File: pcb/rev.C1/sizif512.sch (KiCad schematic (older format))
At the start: 186 parts, among them J1 DS-210, J10 RCJ-014, J11 PinHeader, J12 PJ-313, J13 PinHeader, J14 PinHeader, J15 PJ-313, J16 MEM2055-00-190-01-A, J17 PinHeader, J2 Conn_02x28_Row_Letter_First, J3 PinHeader, J4 DS1020-08, J5 DS1020-05, J6 PinHeader, J7 DB9-M, J8 PinHeader, J9 Mini-DIN-9, Q1 BC547C, Q2 BC547C, Q3 BC547C, Q4 BC547C, SW1 Jumper, SW2 Button THT, SW3 Button THT, U1 LM2596T-ADJ, U10 SN74CB3T3245PW, U11 AD724, U12 AS6C4008-55PCN, U13 74HCT4053D, U14 AY-3-8910, U15 LM311N, U2 AMS1117-3.3, U3 SN74CB3T3245PW, U4 Z84C0010PEC, U5 SN74CB3T3245PW, U6 EPM1270T144, U7 SN74CB3T3245PW, U8 SST39SF040, U9 74HCU04, Y1 28 MHz, Y2 4.433 MHz

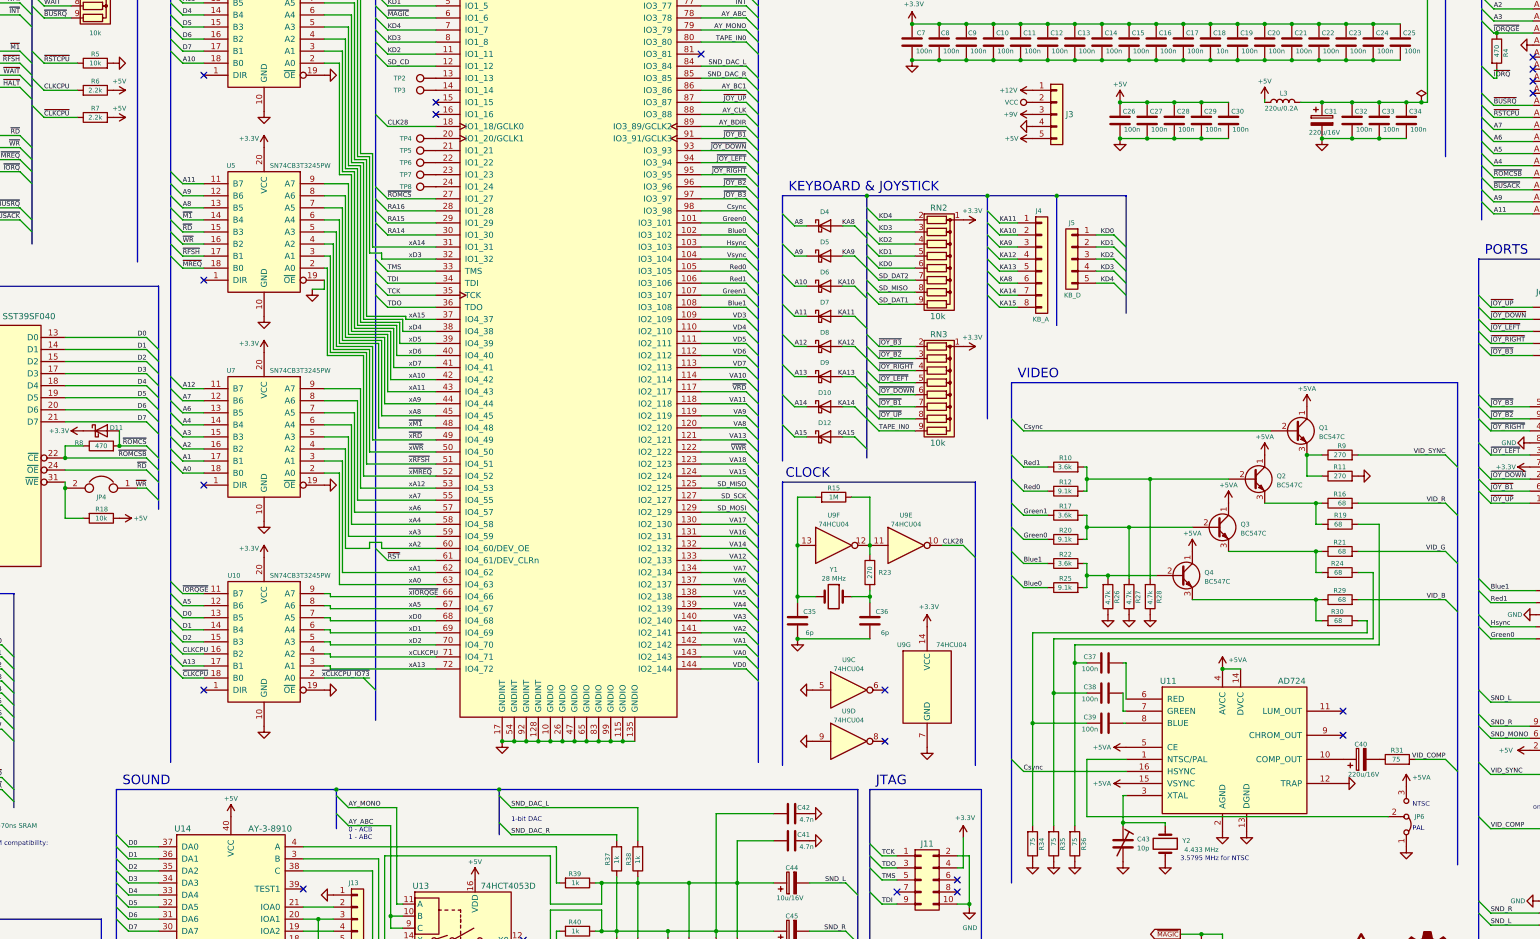
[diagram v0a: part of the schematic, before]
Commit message: pcb rev.C1: minor values change
Video circuit tuning:
R10, R17, R22, R26, R27, R27: 1.5k
R12, R20, R25: 3k
C43: 30p (wider range is better)
Q1, Q2, Q3, Q4: BC549B (low noise, less amplification)

Exclude 2.2k value from BOM:
R6, R7: 2k

Also add some assembly drawing.
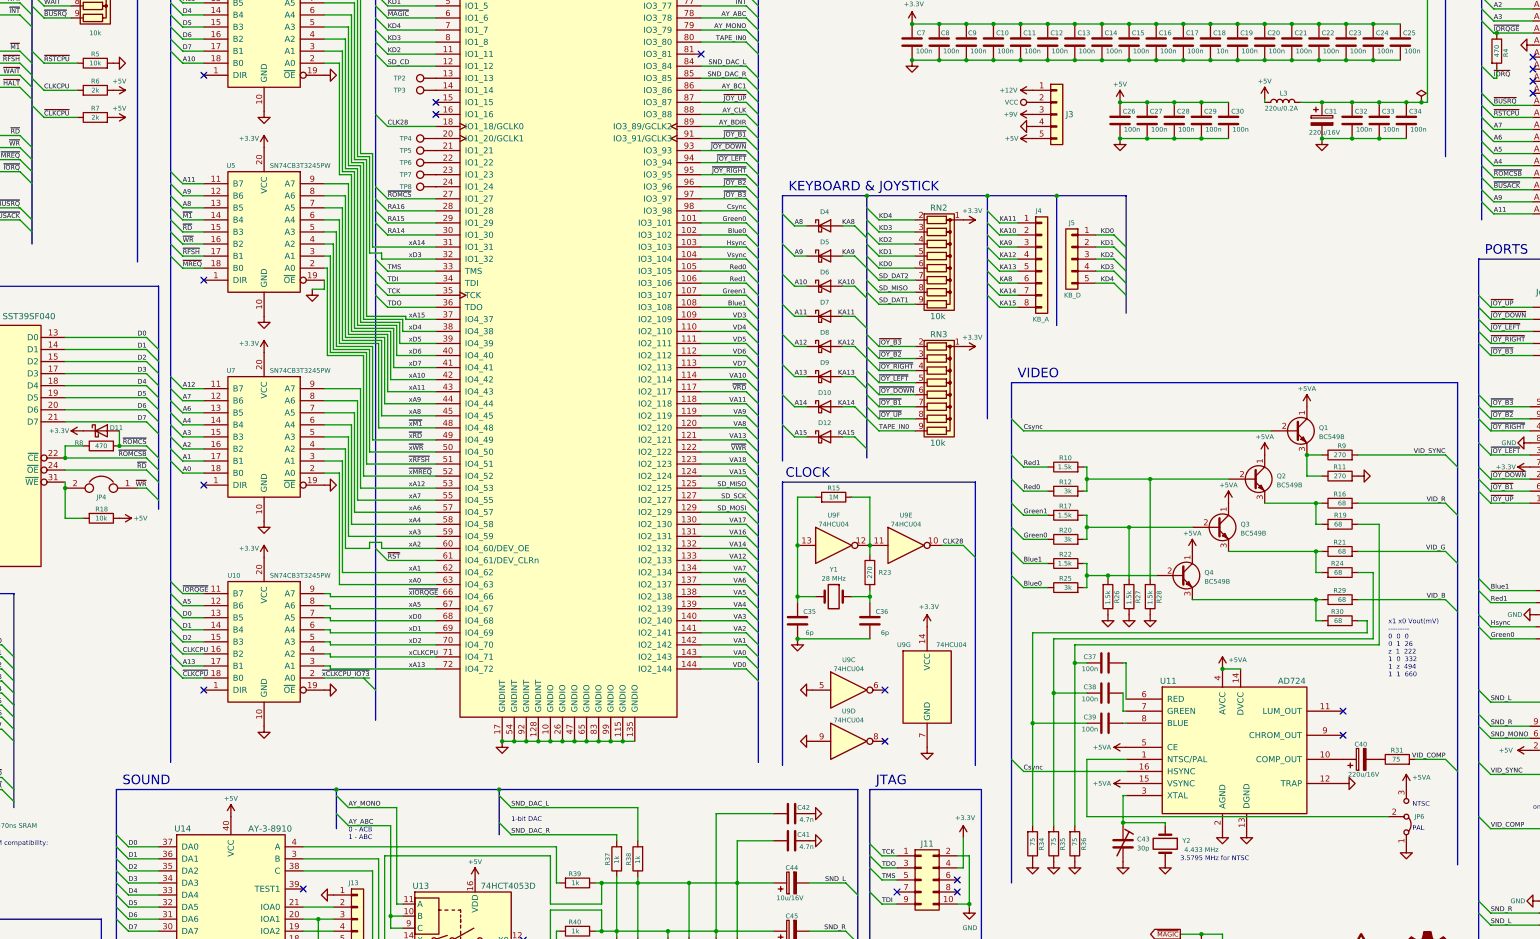
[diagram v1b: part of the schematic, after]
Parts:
- C43: value 10p -> 30p
- Q1, Q2, Q3, Q4: value BC547C -> BC549B
- R10, R17, R22: value 3.6k -> 1.5k
- R12, R20, R25: value 9.1k -> 3k
- R26, R27, R28: value 4.7k -> 1.5k
- R6, R7: value 2.2k -> 2k
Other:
- note added: "x1 x0 Vout(mV)\n---------\n0 0 0\n0 1 26\nz 1 222\n1 0 332\n1 z 494\n1 1 660"
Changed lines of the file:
@@
 P 13050 5300
 F 0 "Q1" H 13250 5325 39  0000 L CNN
-F 1 "BC547C" H 13250 5250 39  0000 L CNN
+F 1 "BC549B" H 13250 5250 39  0000 L CNN
 F 2 "Package_TO_SOT_THT:TO-92_Inline" H 13250 5400 50  0001 C CNN
 F 3 "~" H 13050 5300 50  0001 C CNN
@@
 P 12400 6100
 F 0 "Q3" H 12600 6125 39  0000 L CNN
-F 1 "BC547C" H 12600 6050 39  0000 L CNN
+F 1 "BC549B" H 12600 6050 39  0000 L CNN
 F 2 "Package_TO_SOT_THT:TO-92_Inline" H 12600 6200 50  0001 C CNN
 F 3 "~" H 12400 6100 50  0001 C CNN
@@
 P 12700 5700
 F 0 "Q2" H 12900 5725 39  0000 L CNN
-F 1 "BC547C" H 12900 5650 39  0000 L CNN
+F 1 "BC549B" H 12900 5650 39  0000 L CNN
 F 2 "Package_TO_SOT_THT:TO-92_Inline" H 12900 5800 50  0001 C CNN
 F 3 "~" H 12700 5700 50  0001 C CNN
@@
 P 12100 6500
 F 0 "Q4" H 12300 6525 39  0000 L CNN
-F 1 "BC547C" H 12300 6450 39  0000 L CNN
+F 1 "BC549B" H 12300 6450 39  0000 L CNN
 F 2 "Package_TO_SOT_THT:TO-92_Inline" H 12300 6600 50  0001 C CNN
 F 3 "~" H 12100 6500 50  0001 C CNN
@@
 	1    0    0    -1
 $EndComp
-$Comp
-L Device:R R27
-U 1 1 6AE636A4
-P 11675 6675
-F 0 "R27" V 11750 6625 39  0000 L CNN
-F 1 "4.7k" V 11675 6625 39  0000 L CNN
-F 2 "Resistor_THT:R_Axial_DIN0207_L6.3mm_D2.5mm_P2.54mm_Vertical" V 11605 6675 50  0001 C CNN
-F 3 "~" H 11675 6675 50  0001 C CNN
-	1    11675 6675
-	1    0    0    1
-$EndComp
-$Comp
-L Device:R R28
-U 1 1 6AE638B4
-P 11850 6675
-F 0 "R28" V 11925 6625 39  0000 L CNN
-F 1 "4.7k" V 11850 6625 39  0000 L CNN
-F 2 "Resistor_THT:R_Axial_DIN0207_L6.3mm_D2.5mm_P2.54mm_Vertical" V 11780 6675 50  0001 C CNN
-F 3 "~" H 11850 6675 50  0001 C CNN
-	1    11850 6675
-	1    0    0    1
-$EndComp
-$Comp
-L Device:R R26
-U 1 1 6AE63367
-P 11500 6675
-F 0 "R26" V 11575 6625 39  0000 L CNN
-F 1 "4.7k" V 11500 6625 39  0000 L CNN
-F 2 "Resistor_THT:R_Axial_DIN0207_L6.3mm_D2.5mm_P2.54mm_Vertical" V 11430 6675 50  0001 C CNN
-F 3 "~" H 11500 6675 50  0001 C CNN
-	1    11500 6675
-	1    0    0    1
-$EndComp
-$Comp
-L Device:R R20
-U 1 1 6AE62B90
-P 11150 6200
-F 0 "R20" V 11225 6150 39  0000 L CNN
-F 1 "9.1k" V 11150 6150 39  0000 L CNN
-F 2 "Resistor_THT:R_Axial_DIN0207_L6.3mm_D2.5mm_P2.54mm_Vertical" V 11080 6200 50  0001 C CNN
-F 3 "~" H 11150 6200 50  0001 C CNN
-	1    11150 6200
-	0    -1   -1   0
-$EndComp
-$Comp
-L Device:R R17
-U 1 1 6AD19095
-P 11150 6000
-F 0 "R17" V 11225 5950 39  0000 L CNN
-F 1 "3.6k" V 11150 5950 39  0000 L CNN
-F 2 "Resistor_THT:R_Axial_DIN0207_L6.3mm_D2.5mm_P2.54mm_Vertical" V 11080 6000 50  0001 C CNN
-F 3 "~" H 11150 6000 50  0001 C CNN
-	1    11150 6000
-	0    -1   -1   0
-$EndComp
-$Comp
-L Device:R R10
-U 1 1 68E90A04
-P 11150 5600
-F 0 "R10" V 11225 5550 39  0000 L CNN
-F 1 "3.6k" V 11150 5550 39  0000 L CNN
-F 2 "Resistor_THT:R_Axial_DIN0207_L6.3mm_D2.5mm_P2.54mm_Vertical" V 11080 5600 50  0001 C CNN
-F 3 "~" H 11150 5600 50  0001 C CNN
-	1    11150 5600
-	0    -1   -1   0
-$EndComp
-$Comp
-L Device:R R12
-U 1 1 6AE624FD
-P 11150 5800
-F 0 "R12" V 11225 5750 39  0000 L CNN
-F 1 "9.1k" V 11150 5750 39  0000 L CNN
-F 2 "Resistor_THT:R_Axial_DIN0207_L6.3mm_D2.5mm_P2.54mm_Vertical" V 11080 5800 50  0001 C CNN
-F 3 "~" H 11150 5800 50  0001 C CNN
-	1    11150 5800
-	0    -1   -1   0
-$EndComp
-$Comp
-L Device:R R25
-U 1 1 6AE63033
-P 11150 6600
-F 0 "R25" V 11225 6550 39  0000 L CNN
-F 1 "9.1k" V 11150 6550 39  0000 L CNN
-F 2 "Resistor_THT:R_Axial_DIN0207_L6.3mm_D2.5mm_P2.54mm_Vertical" V 11080 6600 50  0001 C CNN
-F 3 "~" H 11150 6600 50  0001 C CNN
-	1    11150 6600
-	0    -1   -1   0
-$EndComp
-$Comp
-L Device:R R22
-U 1 1 6AE621E9
-P 11150 6400
-F 0 "R22" V 11225 6350 39  0000 L CNN
-F 1 "3.6k" V 11150 6350 39  0000 L CNN
-F 2 "Resistor_THT:R_Axial_DIN0207_L6.3mm_D2.5mm_P2.54mm_Vertical" V 11080 6400 50  0001 C CNN
-F 3 "~" H 11150 6400 50  0001 C CNN
-	1    11150 6400
-	0    -1   -1   0
-$EndComp
 Text Notes 1950 8875 0    39   ~ 0
 For 256K RAM compatibility:\nVA18<->A17\nVA17<->A18
@@
 P 11625 8725
 F 0 "C43" H 11741 8763 39  0000 L CNN
-F 1 "10p" H 11741 8688 39  0000 L CNN
+F 1 "30p" H 11741 8688 39  0000 L CNN
 F 2 "my:C_Trim_D6.3mm_P5.50mm" H 11625 8725 50  0001 C CNN
 F 3 "~" H 11625 8725 50  0001 C CNN
@@
 CLKCPU
 $Comp
-L Device:R R7
-U 1 1 61E034AA
-P 3100 2700
-F 0 "R7" V 3175 2700 39  0000 C CNN
-F 1 "2.2k" V 3100 2700 39  0000 C CNN
-F 2 "Resistor_THT:R_Axial_DIN0207_L6.3mm_D2.5mm_P7.62mm_Horizontal" V 3030 2700 50  0001 C CNN
-F 3 "~" H 3100 2700 50  0001 C CNN
-	1    3100 2700
-	0    -1   -1   0
-$EndComp
-$Comp
 L power:+5V #PWR022
 U 1 1 61EE6901
@@
 	2575 2600 2675 2700
 $Comp
-L Device:R R6
-U 1 1 6438D197
-P 3100 2475
-F 0 "R6" V 3175 2475 39  0000 C CNN
-F 1 "2.2k" V 3100 2475 39  0000 C CNN
-F 2 "Resistor_THT:R_Axial_DIN0207_L6.3mm_D2.5mm_P7.62mm_Horizontal" V 3030 2475 50  0001 C CNN
-F 3 "~" H 3100 2475 50  0001 C CNN
-	1    3100 2475
-	0    1    -1   0
-$EndComp
-$Comp
 L power:+5V #PWR028
 U 1 1 6438D19D
@@
 	-1   0    0    1
 $EndComp
+$Comp
+L Device:R R6
+U 1 1 6438D197
+P 3100 2475
+F 0 "R6" V 3175 2475 39  0000 C CNN
+F 1 "2k" V 3100 2475 39  0000 C CNN
+F 2 "Resistor_THT:R_Axial_DIN0207_L6.3mm_D2.5mm_P7.62mm_Horizontal" V 3030 2475 50  0001 C CNN
+F 3 "~" H 3100 2475 50  0001 C CNN
+	1    3100 2475
+	0    1    -1   0
+$EndComp
+$Comp
+L Device:R R7
+U 1 1 61E034AA
+P 3100 2700
+F 0 "R7" V 3175 2700 39  0000 C CNN
+F 1 "2k" V 3100 2700 39  0000 C CNN
+F 2 "Resistor_THT:R_Axial_DIN0207_L6.3mm_D2.5mm_P7.62mm_Horizontal" V 3030 2700 50  0001 C CNN
+F 3 "~" H 3100 2700 50  0001 C CNN
+	1    3100 2700
+	0    -1   -1   0
+$EndComp
+$Comp
+L Device:R R10
+U 1 1 68E90A04
+P 11150 5600
+F 0 "R10" V 11225 5550 39  0000 L CNN
+F 1 "1.5k" V 11150 5550 39  0000 L CNN
+F 2 "Resistor_THT:R_Axial_DIN0207_L6.3mm_D2.5mm_P2.54mm_Vertical" V 11080 5600 50  0001 C CNN
+F 3 "~" H 11150 5600 50  0001 C CNN
+	1    11150 5600
+	0    -1   -1   0
+$EndComp
+$Comp
+L Device:R R17
+U 1 1 6AD19095
+P 11150 6000
+F 0 "R17" V 11225 5950 39  0000 L CNN
+F 1 "1.5k" V 11150 5950 39  0000 L CNN
+F 2 "Resistor_THT:R_Axial_DIN0207_L6.3mm_D2.5mm_P2.54mm_Vertical" V 11080 6000 50  0001 C CNN
+F 3 "~" H 11150 6000 50  0001 C CNN
+	1    11150 6000
+	0    -1   -1   0
+$EndComp
+$Comp
+L Device:R R22
+U 1 1 6AE621E9
+P 11150 6400
+F 0 "R22" V 11225 6350 39  0000 L CNN
+F 1 "1.5k" V 11150 6350 39  0000 L CNN
+F 2 "Resistor_THT:R_Axial_DIN0207_L6.3mm_D2.5mm_P2.54mm_Vertical" V 11080 6400 50  0001 C CNN
+F 3 "~" H 11150 6400 50  0001 C CNN
+	1    11150 6400
+	0    -1   -1   0
+$EndComp
+$Comp
+L Device:R R12
+U 1 1 6AE624FD
+P 11150 5800
+F 0 "R12" V 11225 5750 39  0000 L CNN
+F 1 "3k" V 11150 5750 39  0000 L CNN
+F 2 "Resistor_THT:R_Axial_DIN0207_L6.3mm_D2.5mm_P2.54mm_Vertical" V 11080 5800 50  0001 C CNN
+F 3 "~" H 11150 5800 50  0001 C CNN
+	1    11150 5800
+	0    -1   -1   0
+$EndComp
+$Comp
+L Device:R R20
+U 1 1 6AE62B90
+P 11150 6200
+F 0 "R20" V 11225 6150 39  0000 L CNN
+F 1 "3k" V 11150 6150 39  0000 L CNN
+F 2 "Resistor_THT:R_Axial_DIN0207_L6.3mm_D2.5mm_P2.54mm_Vertical" V 11080 6200 50  0001 C CNN
+F 3 "~" H 11150 6200 50  0001 C CNN
+	1    11150 6200
+	0    -1   -1   0
+$EndComp
+$Comp
+L Device:R R25
+U 1 1 6AE63033
+P 11150 6600
+F 0 "R25" V 11225 6550 39  0000 L CNN
+F 1 "3k" V 11150 6550 39  0000 L CNN
+F 2 "Resistor_THT:R_Axial_DIN0207_L6.3mm_D2.5mm_P2.54mm_Vertical" V 11080 6600 50  0001 C CNN
+F 3 "~" H 11150 6600 50  0001 C CNN
+	1    11150 6600
+	0    -1   -1   0
+$EndComp
+$Comp
+L Device:R R26
+U 1 1 6AE63367
+P 11500 6675
+F 0 "R26" V 11575 6625 39  0000 L CNN
+F 1 "1.5k" V 11500 6625 39  0000 L CNN
+F 2 "Resistor_THT:R_Axial_DIN0207_L6.3mm_D2.5mm_P2.54mm_Vertical" V 11430 6675 50  0001 C CNN
+F 3 "~" H 11500 6675 50  0001 C CNN
+	1    11500 6675
+	1    0    0    1
+$EndComp
+$Comp
+L Device:R R27
+U 1 1 6AE636A4
+P 11675 6675
+F 0 "R27" V 11750 6625 39  0000 L CNN
+F 1 "1.5k" V 11675 6625 39  0000 L CNN
+F 2 "Resistor_THT:R_Axial_DIN0207_L6.3mm_D2.5mm_P2.54mm_Vertical" V 11605 6675 50  0001 C CNN
+F 3 "~" H 11675 6675 50  0001 C CNN
+	1    11675 6675
+	1    0    0    1
+$EndComp
+$Comp
+L Device:R R28
+U 1 1 6AE638B4
+P 11850 6675
+F 0 "R28" V 11925 6625 39  0000 L CNN
+F 1 "1.5k" V 11850 6625 39  0000 L CNN
+F 2 "Resistor_THT:R_Axial_DIN0207_L6.3mm_D2.5mm_P2.54mm_Vertical" V 11780 6675 50  0001 C CNN
+F 3 "~" H 11850 6675 50  0001 C CNN
+	1    11850 6675
+	1    0    0    1
+$EndComp
 Wire Wire Line
 	5000 7350 5375 7350
@@
 Wire Bus Line
 	8600 575  8600 8050
+Text Notes 13825 7350 0    39   ~ 0
+x1 x0 Vout(mV)\n---------\n0  0  0\n0  1  26\nz  1  222\n1  0  332\n1  z  494\n1  1  660
 $EndSCHEMATC

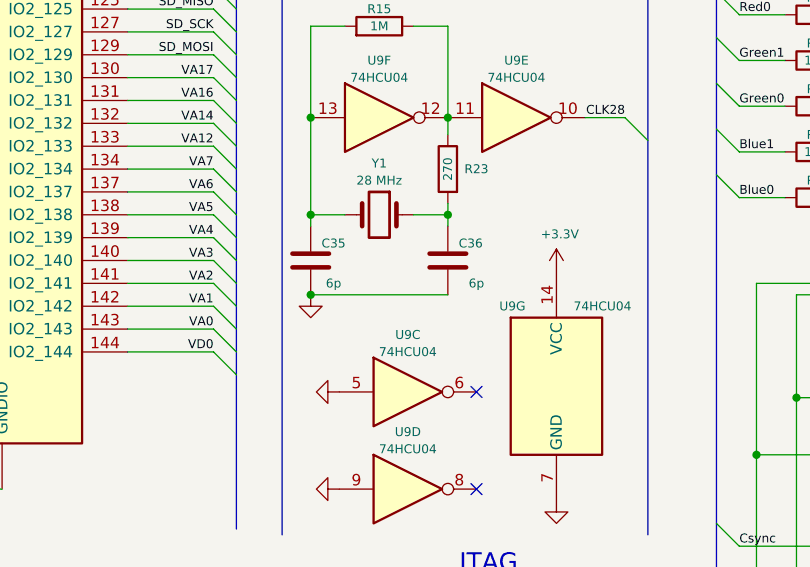
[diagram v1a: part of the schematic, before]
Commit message: pcb rev.C1: update Y1 capacitors values for better reliability
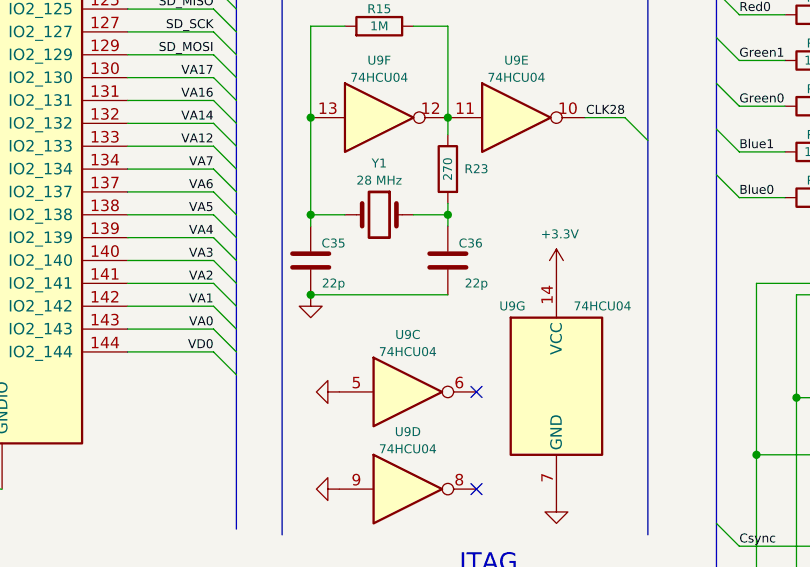
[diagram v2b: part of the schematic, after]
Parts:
- C35, C36: value 6p -> 22p
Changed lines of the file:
@@
 P 9525 6875
 F 0 "C36" H 9425 6800 39  0000 C CNN
-F 1 "6p" H 9400 6975 39  0000 C CNN
+F 1 "22p" H 9400 6975 39  0000 C CNN
 F 2 "Capacitor_THT:C_Disc_D3.8mm_W2.6mm_P2.50mm" H 9563 6725 50  0001 C CNN
 F 3 "~" H 9525 6875 50  0001 C CNN
@@
 P 8925 6875
 F 0 "C35" H 8825 6800 39  0000 C CNN
-F 1 "6p" H 8825 6975 39  0000 C CNN
+F 1 "22p" H 8825 6975 39  0000 C CNN
 F 2 "Capacitor_THT:C_Disc_D3.8mm_W2.6mm_P2.50mm" H 8963 6725 50  0001 C CNN
 F 3 "~" H 8925 6875 50  0001 C CNN
@@
 	1    0    0    1
 $EndComp
+Text Notes 13825 7350 0    39   ~ 0
+x1 x0 Vout(mV)\n---------\n0  0  0\n0  1  26\nz  1  222\n1  0  332\n1  z  494\n1  1  660
 Wire Wire Line
 	5000 7350 5375 7350
@@
 Wire Bus Line
 	8600 575  8600 8050
-Text Notes 13825 7350 0    39   ~ 0
-x1 x0 Vout(mV)\n---------\n0  0  0\n0  1  26\nz  1  222\n1  0  332\n1  z  494\n1  1  660
 $EndSCHEMATC
